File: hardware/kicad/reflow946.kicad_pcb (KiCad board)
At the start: 2 copper layers, 104 x 60 mm, 56 parts, among them J1 VH-2A, J2 VH-3A2, J3 VH-3A2, J4 XH-A2, J5 HDR-M-2.54_2x3, Q1 BTA16-600BRG, Q2 MMBT3906, Q3 MMBT3906, Q4 MMBT3906, SW1 SW_Push, SW2 SW_Push, SW3 SW_Push, U1 MOC3041M, U2 ESP32-WROOM-32U, U3 MAX31855KASA, U4 AMS1117-3.3

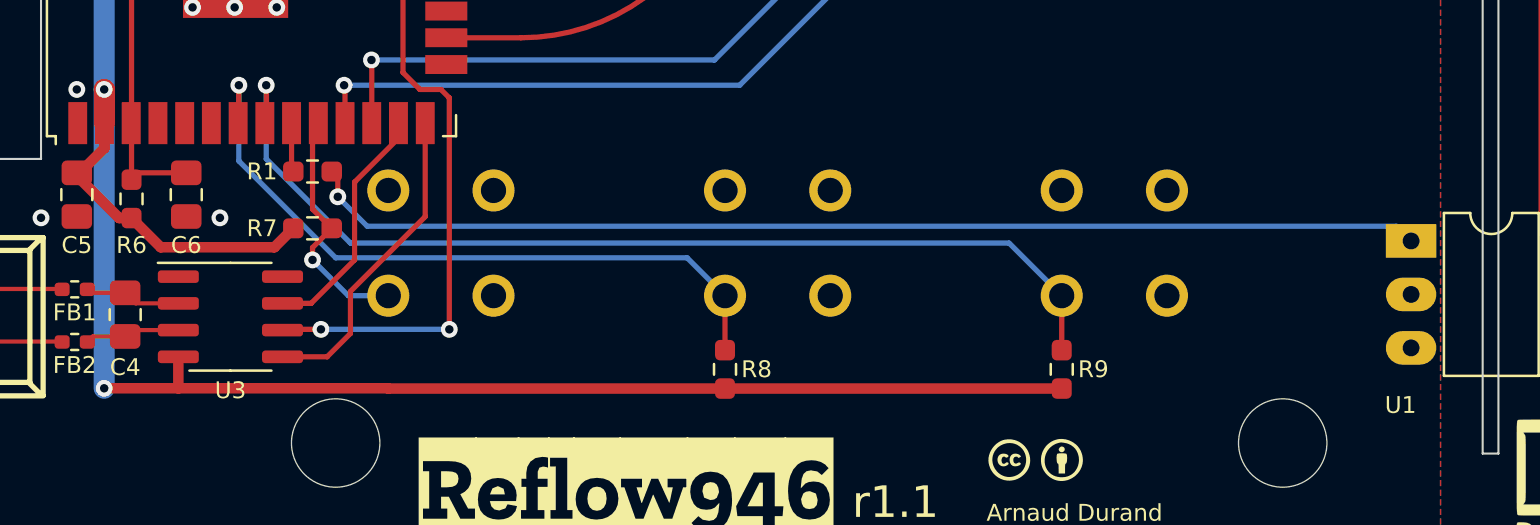
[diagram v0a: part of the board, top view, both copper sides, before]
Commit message: Fix wrong pinout on push buttons
Leaving pull up resistor footprints in place, so they can be populated
if needed.
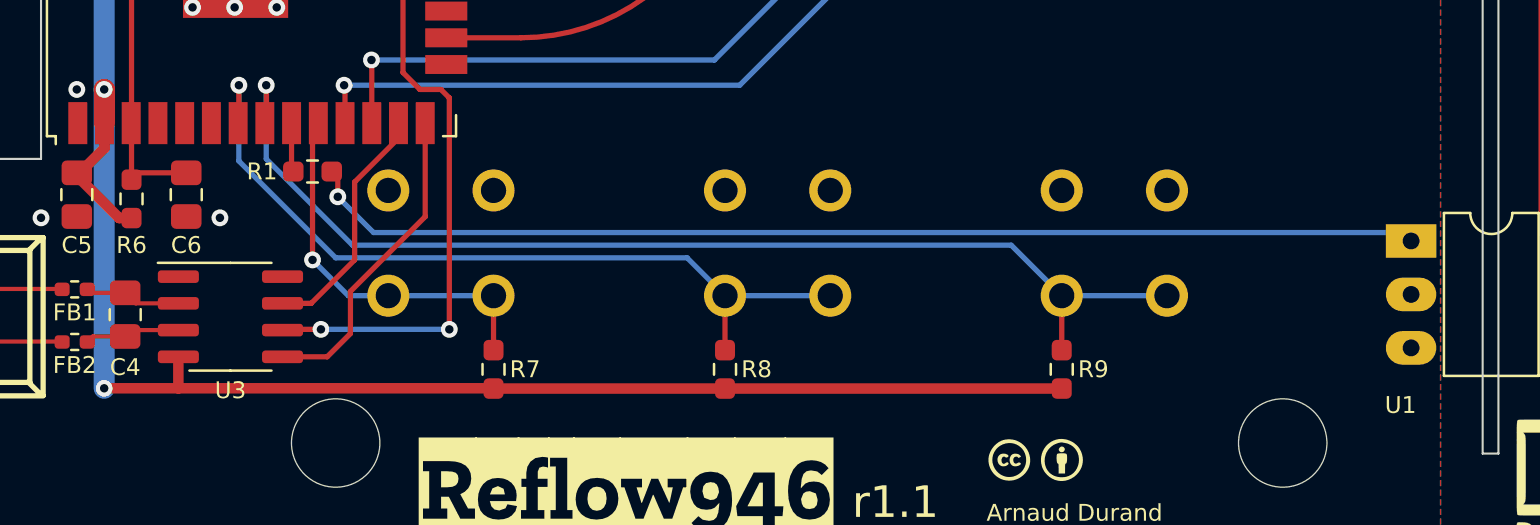
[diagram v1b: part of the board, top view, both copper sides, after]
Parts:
- moved R7 10.9 mm to (127.5, 120.0), turned to -90 degrees
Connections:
- SW1 pad 1: GND -> /button1
- SW1 pad 2: /button1 -> GND
- SW2 pad 1: GND -> /button2
- SW2 pad 2: /button2 -> GND
- SW3 pad 1: GND -> /button3
- SW3 pad 2: /button3 -> GND
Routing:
- net +3.3V: track 152.6 -> 144.0 mm
- net /button3: track 11.7 -> 18.5 mm
- net /button2: track 33.8 -> 38.8 mm
- net /button1: track 48.4 -> 53.4 mm
